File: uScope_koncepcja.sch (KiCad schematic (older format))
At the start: 19 parts

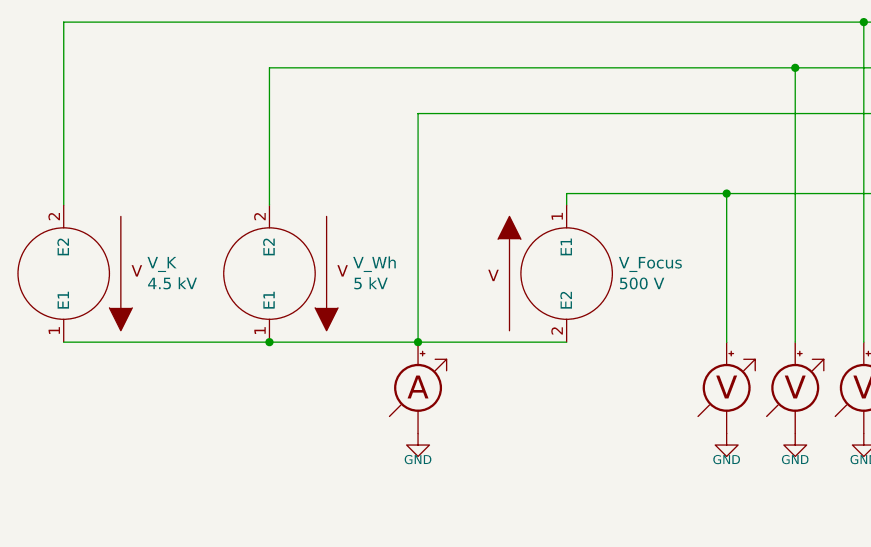
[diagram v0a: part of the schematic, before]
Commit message: - schematic as hierarchical - added cache lib
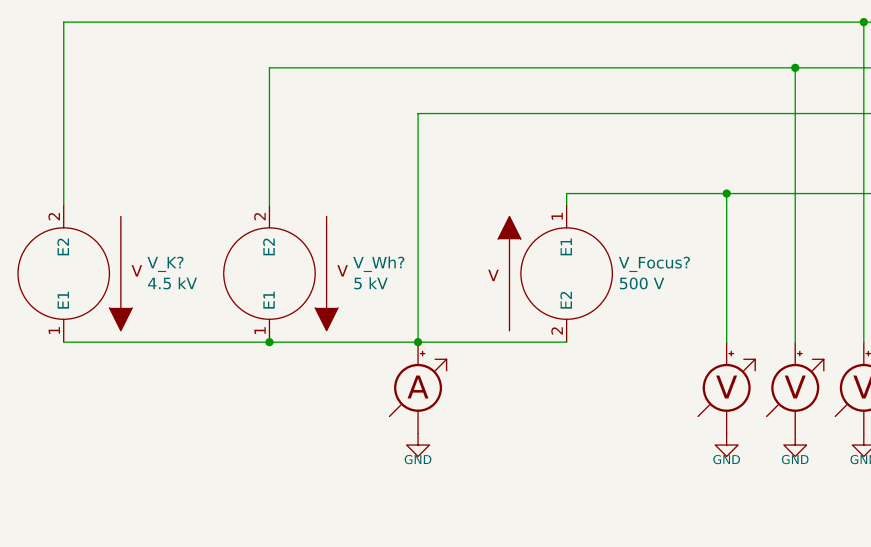
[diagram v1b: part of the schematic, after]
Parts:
- renumbered V_Focus to V_Focus?, V_K to V_K?, V_Wh to V_Wh?
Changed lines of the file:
@@
 EESchema Schematic File Version 4
+LIBS:uScope-cache
 EELAYER 26 0
 EELAYER END
 $Descr A4 11693 8268
 encoding utf-8
-Sheet 1 1
+Sheet 2 5
 Title ""
 Date "2020-08-14"
@@
 $EndComp
 $Comp
-L pspice:VSOURCE V_K
+L pspice:VSOURCE V_K?
 U 1 1 5F36B478
 P 1250 2300
-F 0 "V_K" H 884 2254 50  0000 R CNN
+F 0 "V_K?" H 884 2254 50  0000 R CNN
 F 1 "4.5 kV" H 884 2345 50  0000 R CNN
 F 2 "" H 1250 2300 50  0001 C CNN
@@
 $EndComp
 $Comp
-L pspice:VSOURCE V_Wh
+L pspice:VSOURCE V_Wh?
 U 1 1 5F36B607
 P 2150 2300
-F 0 "V_Wh" H 1784 2254 50  0000 R CNN
+F 0 "V_Wh?" H 1784 2254 50  0000 R CNN
 F 1 "5 kV" H 1784 2345 50  0000 R CNN
 F 2 "" H 2150 2300 50  0001 C CNN
@@
 $EndComp
 $Comp
-L pspice:VSOURCE V_Focus
+L pspice:VSOURCE V_Focus?
 U 1 1 5F36B645
 P 3450 2300
-F 0 "V_Focus" H 3678 2346 50  0000 L CNN
+F 0 "V_Focus?" H 3678 2346 50  0000 L CNN
 F 1 "500 V" H 3678 2255 50  0000 L CNN
 F 2 "" H 3450 2300 50  0001 C CNN

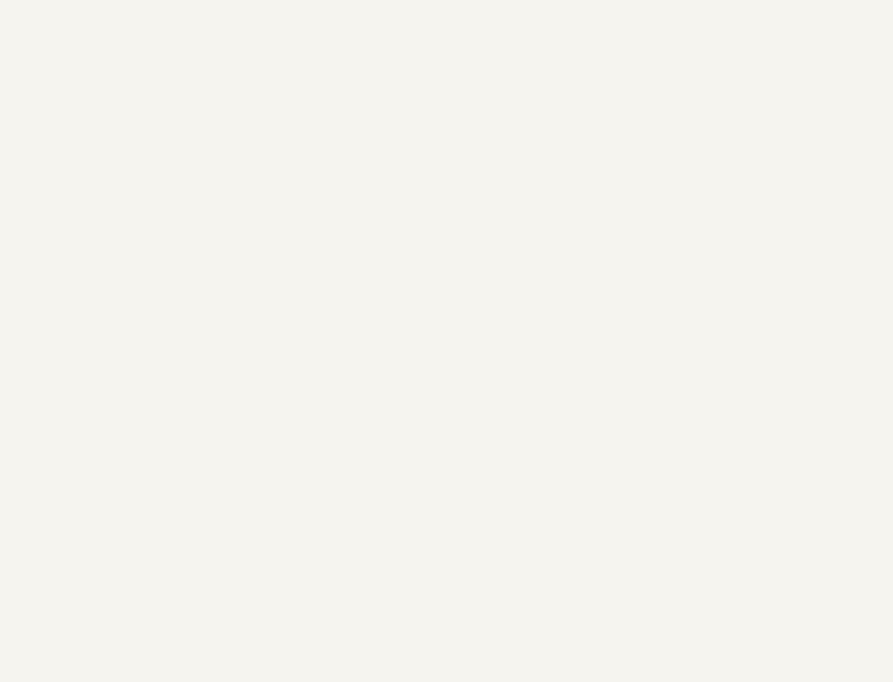
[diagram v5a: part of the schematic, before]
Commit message: - supply converter develop - added sheet: MCU - cleanup 'koncepcja' sub-schematics
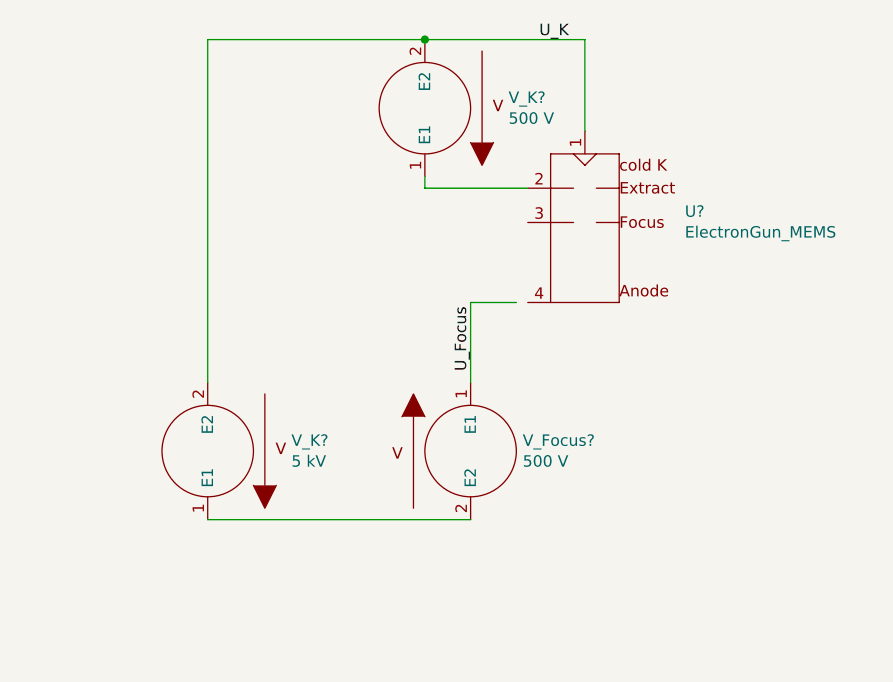
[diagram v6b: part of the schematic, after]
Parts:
- added U?: ElectronGun_MEMS, symbol uScope:ElectronGun_MEMS
- added V_Focus?, V_K?: 500 V, symbol pspice:VSOURCE
- added V_K?: 5 kV, symbol pspice:VSOURCE
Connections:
- net labels added: U_Focus, U_K
- wire segments 35 -> 44
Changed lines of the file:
@@
 $Descr A4 11693 8268
 encoding utf-8
-Sheet 2 10
+Sheet 2 9
 Title ""
 Date "2020-08-14"
@@
 	1    0    0    -1
 $EndComp
+$Comp
+L pspice:VSOURCE V_K?
+U 1 1 5F8FB35A
+P 9050 1300
+AR Path="/5F40DB43/5F8FB35A" Ref="V_K?"  Part="1"
+AR Path="/5F40D708/5F8FB35A" Ref="V_K?"  Part="1"
+F 0 "V_K?" H 8684 1254 50  0000 R CNN
+F 1 "500 V" H 8684 1345 50  0000 R CNN
+F 2 "" H 9050 1300 50  0001 C CNN
+F 3 "~" H 9050 1300 50  0001 C CNN
+	1    9050 1300
+	-1   0    0    1
+$EndComp
+$Comp
+L pspice:VSOURCE V_K?
+U 1 1 5F8FB361
+P 8100 2800
+AR Path="/5F40DB43/5F8FB361" Ref="V_K?"  Part="1"
+AR Path="/5F40D708/5F8FB361" Ref="V_K?"  Part="1"
+F 0 "V_K?" H 7734 2754 50  0000 R CNN
+F 1 "5 kV" H 7734 2845 50  0000 R CNN
+F 2 "" H 8100 2800 50  0001 C CNN
+F 3 "~" H 8100 2800 50  0001 C CNN
+	1    8100 2800
+	-1   0    0    1
+$EndComp
+$Comp
+L pspice:VSOURCE V_Focus?
+U 1 1 5F8FB368
+P 9250 2800
+AR Path="/5F40DB43/5F8FB368" Ref="V_Focus?"  Part="1"
+AR Path="/5F40D708/5F8FB368" Ref="V_Focus?"  Part="1"
+F 0 "V_Focus?" H 9478 2846 50  0000 L CNN
+F 1 "500 V" H 9478 2755 50  0000 L CNN
+F 2 "" H 9250 2800 50  0001 C CNN
+F 3 "~" H 9250 2800 50  0001 C CNN
+	1    9250 2800
+	1    0    0    -1
+$EndComp
+Wire Wire Line
+	9250 2150 9250 2500
+Wire Wire Line
+	8100 1000 8100 2500
+Wire Wire Line
+	9450 2150 9250 2150
+Text Label 9550 1000 0    50   ~ 0
+U_K
+Text Label 9250 2450 1    50   ~ 0
+U_Focus
+Wire Wire Line
+	8100 1000 9050 1000
+Wire Wire Line
+	9750 1000 9750 1400
+$Comp
+L uScope:ElectronGun_MEMS U?
+U 1 1 5F8FB376
+P 9750 1950
+AR Path="/5F40DB43/5F8FB376" Ref="U?"  Part="1"
+AR Path="/5F40D708/5F8FB376" Ref="U?"  Part="1"
+F 0 "U?" H 10187 2148 50  0000 L CNN
+F 1 "ElectronGun_MEMS" H 10187 2057 50  0000 L CNN
+F 2 "" H 9750 1450 50  0001 C CNN
+F 3 "" H 9750 1450 50  0001 C CNN
+	1    9750 1950
+	1    0    0    -1
+$EndComp
+Wire Wire Line
+	8100 3100 9250 3100
+Connection ~ 9050 1000
+Wire Wire Line
+	9050 1000 9750 1000
+Wire Wire Line
+	9500 1650 9050 1650
+Wire Wire Line
+	9050 1650 9050 1600
 $EndSCHEMATC

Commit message: - changes..
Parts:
- removed MES? (x5): Amperemeter_DC, symbol Device:Amperemeter_DC
- removed MES? (x6): Voltmeter_DC, symbol Device:Voltmeter_DC
- removed U? (x2): ElectronGun, symbol uScope:ElectronGun
- removed U?: ElectronGun_MEMS, symbol uScope:ElectronGun_MEMS
- removed V_Focus? (x3), V_K?: 500 V, symbol pspice:VSOURCE
- removed V_K? (x2): 4.5 kV, symbol pspice:VSOURCE
- removed V_K?, V_Wh? (x2): 5 kV, symbol pspice:VSOURCE
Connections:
- net labels removed: GND, U_Focus, U_K
- wire segments 44 -> 0
